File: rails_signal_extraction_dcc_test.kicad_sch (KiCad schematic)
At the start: 1 part, among them J201 Conn_02x02_Odd_Even

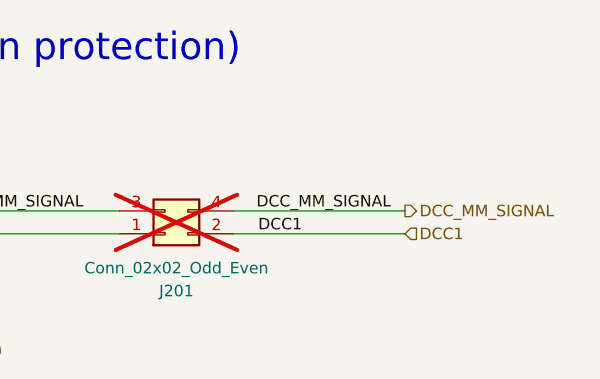
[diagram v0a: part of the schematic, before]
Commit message: Fix - rail_signal_extract (ERC)
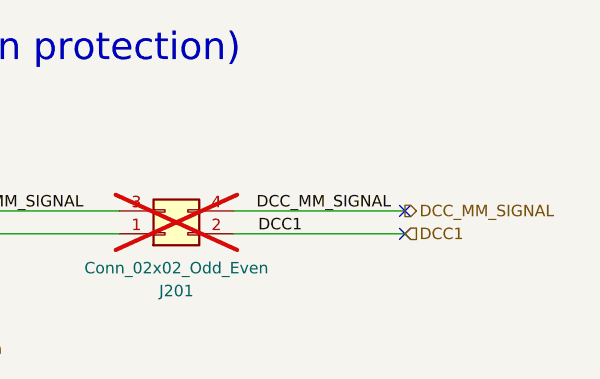
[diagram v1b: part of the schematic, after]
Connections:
- no-connect marks 0 -> 2
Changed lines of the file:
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@@
 		(company "Chatelain Engineering, Bern - CH")
+	)
+	(no_connect
+		(at 148.59 44.45)
+	)
+	(no_connect
+		(at 148.59 46.99)
 	)
 	(wire
@@
 	(label "J_DCC1"
 		(at 96.52 46.99 0)
-		(fields_autoplaced yes)
 		(effects
 			(font
@@
 	(label "J_DCC1"
 		(at 55.88 46.99 0)
-		(fields_autoplaced yes)
 		(effects
 			(font
@@
 	(label "DCC_MM_SIGNAL"
 		(at 132.08 44.45 0)
-		(fields_autoplaced yes)
 		(effects
 			(font
@@
 	(label "DCC1"
 		(at 137.16 46.99 180)
-		(fields_autoplaced yes)
 		(effects
 			(font
@@
 	(label "J_DCC_MM_SIGNAL"
 		(at 96.52 44.45 0)
-		(fields_autoplaced yes)
 		(effects
 			(font
@@
 		(shape input)
 		(at 148.59 46.99 0)
-		(fields_autoplaced yes)
 		(effects
 			(font
@@
 		(shape output)
 		(at 148.59 44.45 0)
-		(fields_autoplaced yes)
 		(effects
 			(font
@@
 		)
 		(instances
-			(project "rails_signal_extraction_dcc-test"
+			(project "rails_signal_extraction_dcc_test"
 				(path "/f9a870df-aaf2-427d-b524-30792058699c"
 					(page "2")
